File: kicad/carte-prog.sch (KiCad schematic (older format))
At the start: 5 parts, among them J1 Connecteur côté carte, J2 RJ12 - Côté ordinateur, J3 3.3V, J4 5V, J5 ALIM

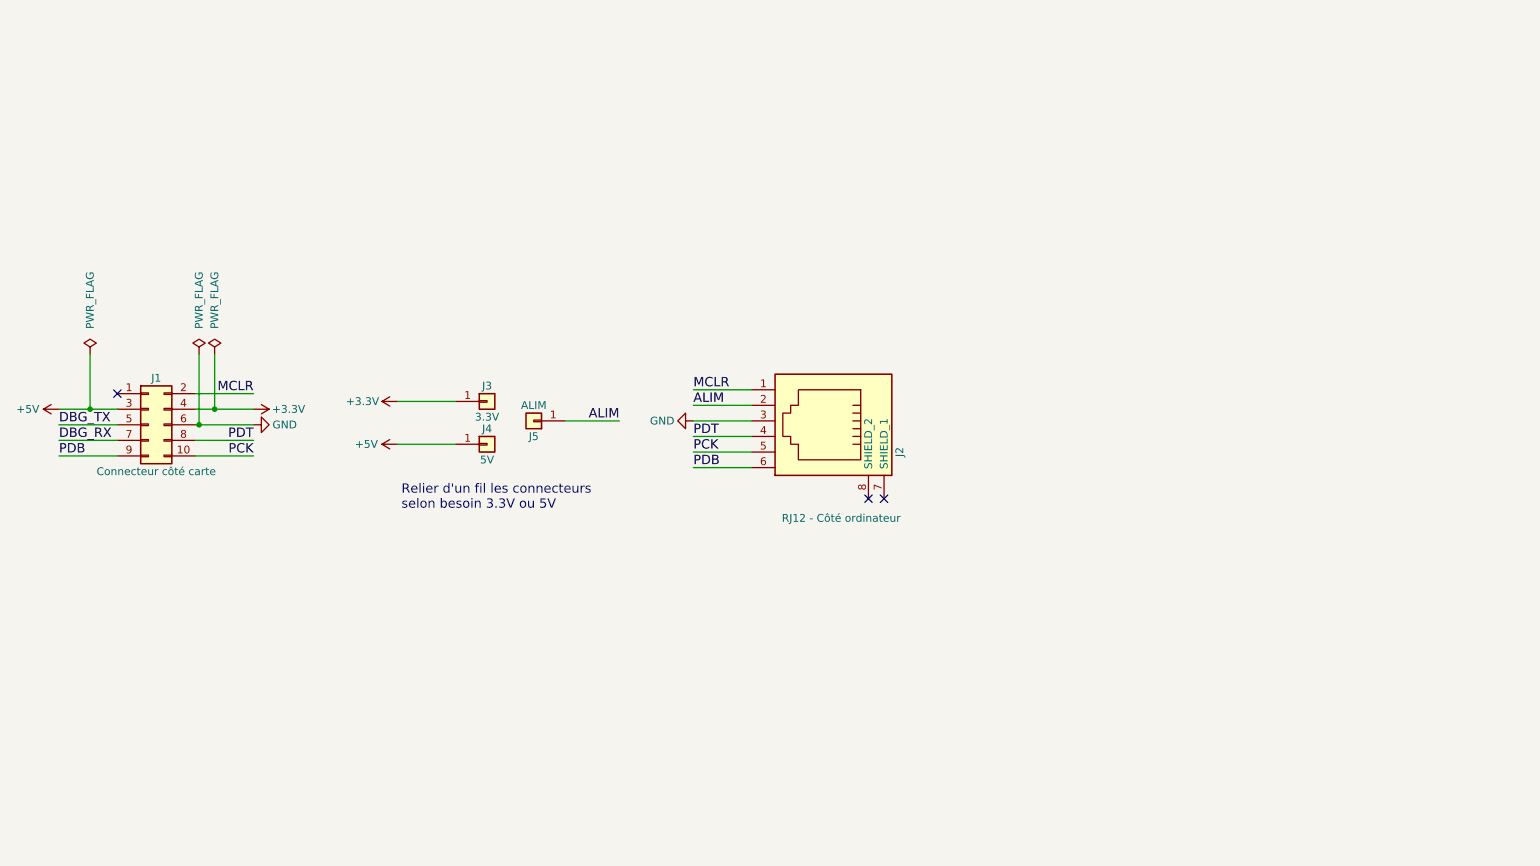
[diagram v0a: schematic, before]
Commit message: Ajout d'un max232
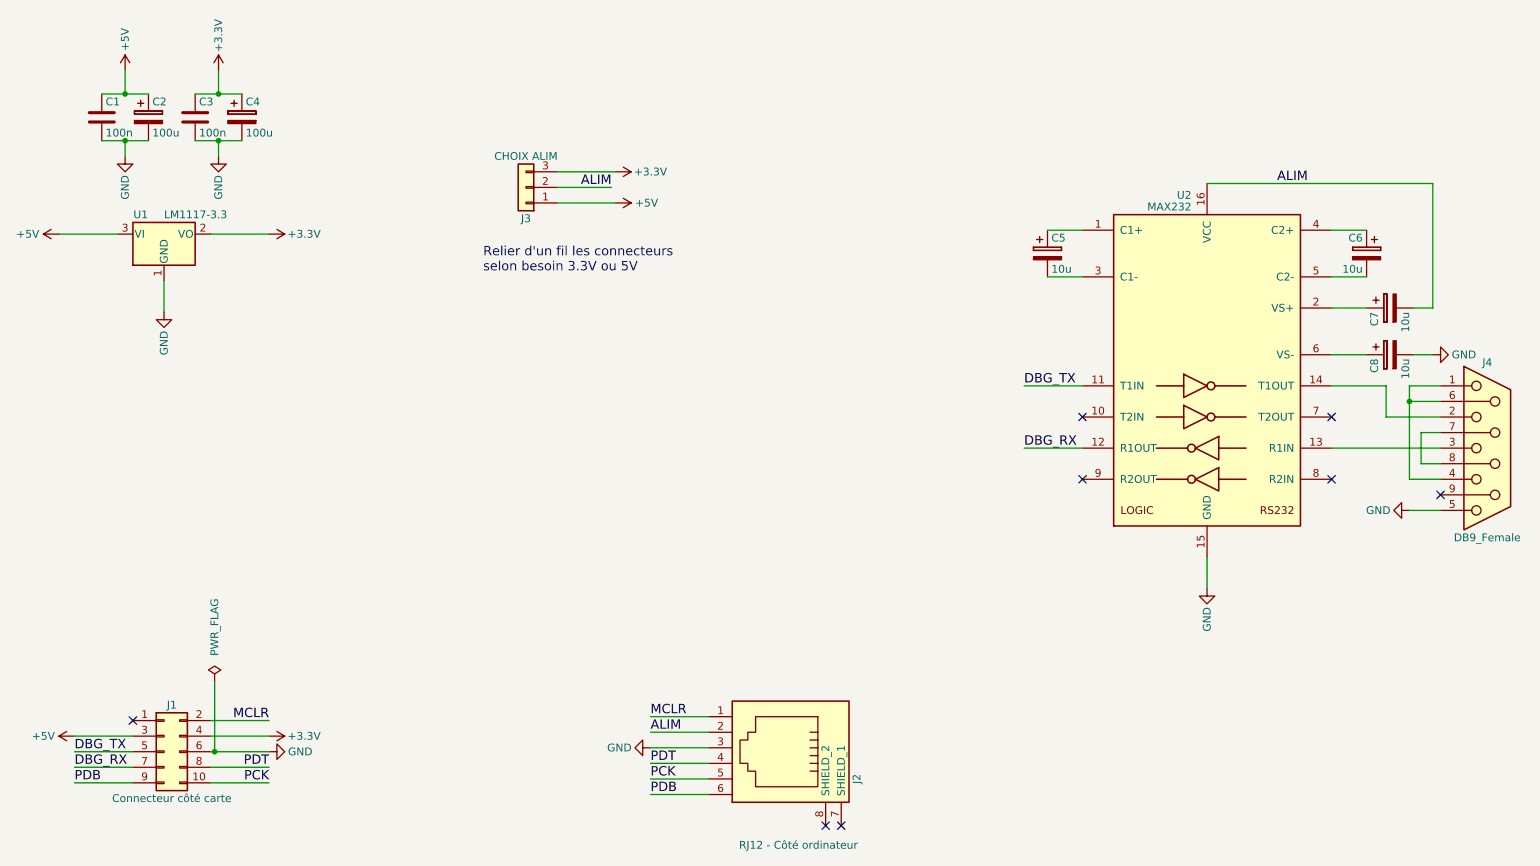
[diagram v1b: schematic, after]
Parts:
- removed J3: 3.3V, Pin_Headers:Pin_Header_Angled_1x01_Pitch2.54mm, symbol Conn_01x01
- removed J4: 5V, Pin_Headers:Pin_Header_Angled_1x01_Pitch2.54mm, symbol Conn_01x01
- removed J5: ALIM, Pin_Headers:Pin_Header_Angled_1x01_Pitch2.54mm, symbol Conn_01x01
- added C1, C3: 100n, Capacitors_THT:C_Rect_L4.0mm_W2.5mm_P2.50mm, symbol C
- added C2, C4: 100u, Capacitors_THT:CP_Radial_D5.0mm_P2.50mm, symbol CP
- added C5, C6, C7, C8: 10u, Capacitors_THT:CP_Radial_D5.0mm_P2.50mm, symbol CP
- added J3: CHOIX ALIM, Pin_Headers:Pin_Header_Angled_1x03_Pitch2.54mm, symbol Conn_01x03
- added J4: DB9_Female, Connectors:DB9FC, symbol DB9_Female
- added U1: LM1117-3.3, TO_SOT_Packages_THT:TO-220_Horizontal, symbol LM1117-3.3
- added U2: MAX232, Housings_DIP:DIP-16_W7.62mm, symbol MAX232
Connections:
- net +3V3: now also C3.1, C4.1, J3.3 (Pin_3), U1.2 (VO)
- net +5V: now also C1.1, C2.1, J3.1 (Pin_1), U1.3 (VI)
- net ALIM: now also C7.2, J3.2 (Pin_2), U2.16 (VCC)
- net DBG_RX: now also U2.12 (R1OUT)
- net DBG_TX: now also U2.11 (T1IN)
- net GND: now also C1.2, C2.2, C3.2, C4.2, C8.2, J4.5, U1.1 (GND), U2.15 (GND)
- new net: C5.1, U2.1 (C1+)
- new net: J4.3, U2.13 (R1IN)
- new net: J4.2, U2.14 (T1OUT)
- new net: C7.1, U2.2 (VS+)
- new net: C5.2, U2.3 (C1-)
- new net: C6.1, U2.4 (C2+)
- new net: C6.2, U2.5 (C2-)
- new net: C8.1, U2.6 (VS-)
- new net: J4.1, J4.4, J4.6
- new net: J4.7, J4.8
- no-connect marks 3 -> 8
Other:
- moved on the sheet: J1, J2

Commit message: Modification des caches
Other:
- note added: "Alimentation depuis ordi"
- note added: "Connecteur côté carte"
- note added: "Connecteur programmation"
- note added: "Debugger"
- note added: "Régulation tension"
- moved on the sheet: C5, C6, C7, C8, J1, J2, J3, J4, U2
